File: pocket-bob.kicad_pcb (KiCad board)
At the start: 2 copper layers, 104.1 x 58.4 mm, 131 parts, among them J3 Conn_01x18, J4 Conn_01x18, J5 Conn_01x18, J6 Conn_01x18, J7 USB_A, P1 Conn_02x18_Odd_Even, P2 Conn_02x18_Odd_Even, U1 TPD3S014

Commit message: Some finishing touches
Remove VIN_USB LED.
Give resistors and LEDs some values.
Update the pours.
Update the silkscreen with board revision.
Update all plots.

Signed-off-by: Michael Welling <mwelling79@gmail.com>
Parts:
- removed D4: LED, LED_SMD:LED_0402_1005Metric
- removed R4: R, Resistor_SMD:R_0402_1005Metric
- D1, D25, D30, D43, D45, D48: value LED -> RED
- D10, D11, D12, D13, D14, D15, D16, D17, D18, D19, D20, D21, D22, D23, D24, D27, D28, D31, D32, D33, D34, D35, D36, D37, D38, D39, D40, D41, D42, D46, D49, D50, D51, D52, D53, D54, D55, D56, D57, D58, D59, D63, D64, D65, D66, D68, D69, D70, D71, D72: value LED -> GREEN
- R1: value R -> 2.2K
- R10, R11, R12, R13, R14, R15, R16, R17, R18, R19, R20, R21, R22, R23, R24, R25, R27, R28, R30, R31, R32, R33, R34, R35, R36, R37, R38, R39, R40, R41, R42, R43, R45, R46, R48, R49, R50, R51, R52, R53, R54, R55, R56, R57, R58, R59, R63, R64, R65, R66, R68, R69, R70, R71, R72: value R -> 1K
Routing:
- net /VIN_USB: track 18.7 -> 16.3 mm
- net Net-(D4-A): track 1.52 -> 0.00 mm
- net GND: track 73.2 -> 72.0 mm, vias 61 -> 60
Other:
- board text added: "Pocket-BoB"
- board text added: "R0 - 03/2025"
- board text added: "m_w"

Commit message: Small updates
Switched all 5V LED current limiting resistors to 2.2K.
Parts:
- R25, R48: value 1K -> 2.2K
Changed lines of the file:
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@@
 			)
 		)
-		(property "Value" "1K"
+		(property "Value" "2.2K"
 			(at 0 1.17 0)
 			(layer "F.Fab")
@@
 			)
 		)
-		(property "Value" "1K"
+		(property "Value" "2.2K"
 			(at 0 1.17 0)
 			(layer "F.Fab")

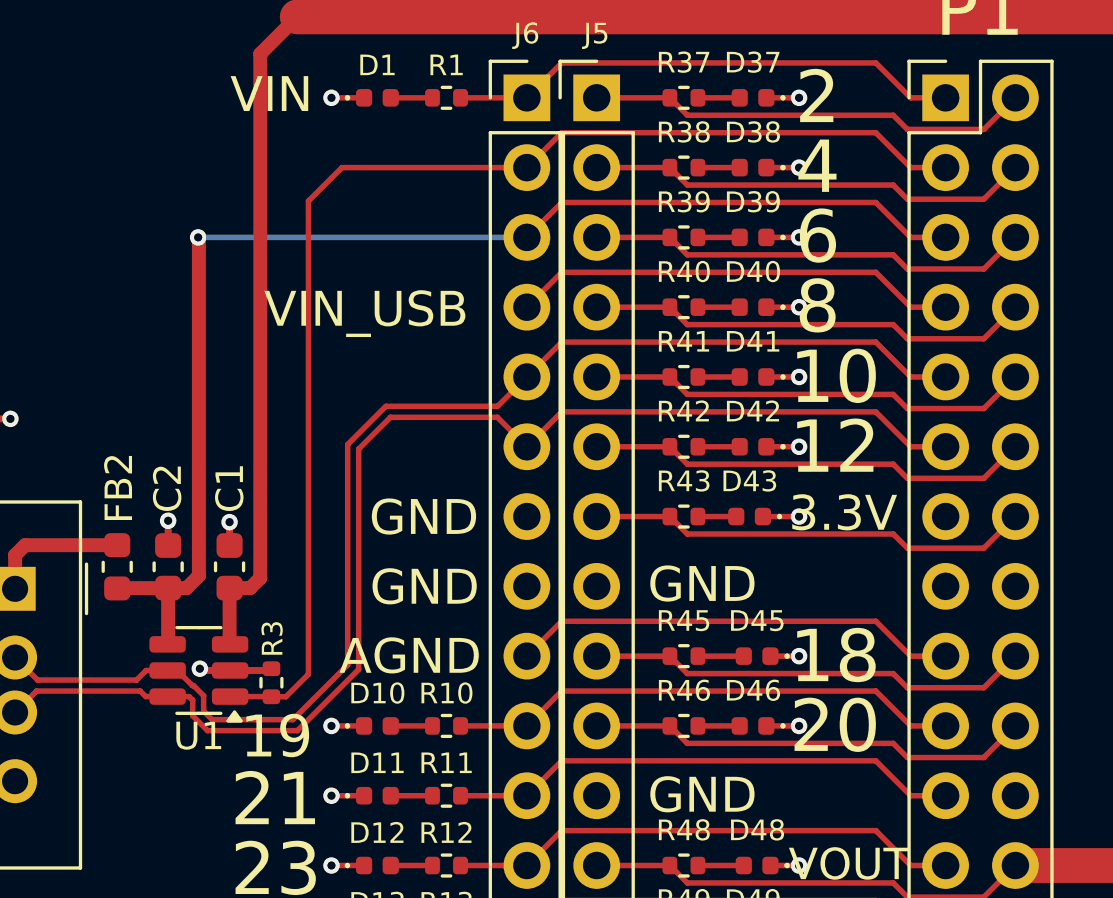
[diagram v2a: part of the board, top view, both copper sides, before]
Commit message: Switch P1_13 to LED instead of GND
The USB_ID functionality is not need if we aren't using OTG.

Signed-off-by: Michael Welling <mwelling79@gmail.com>
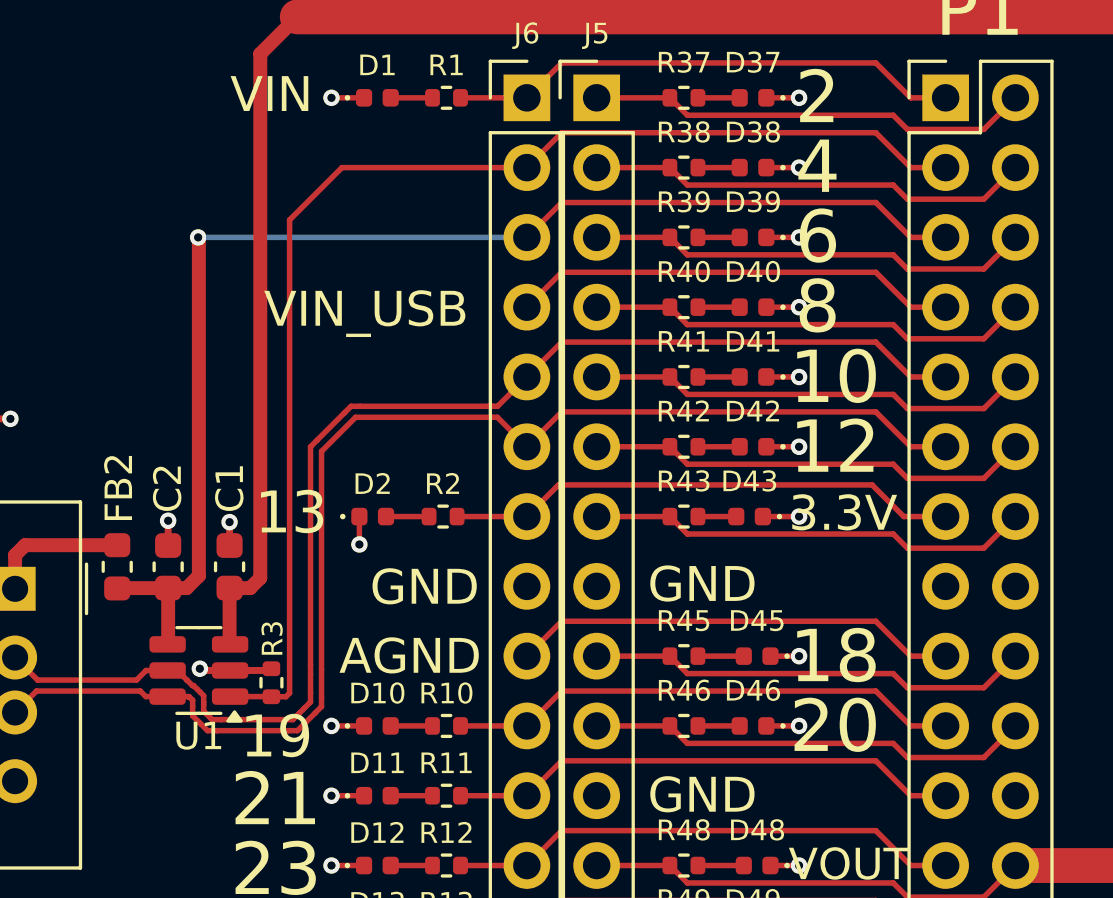
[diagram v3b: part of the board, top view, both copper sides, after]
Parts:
- added D2: GREEN, LED_SMD:LED_0402_1005Metric, F.Cu at (60.4, 83.8)
- added R2: 1K, Resistor_SMD:R_0402_1005Metric, F.Cu at (63.0, 83.8)
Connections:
- J6 pad 7: GND -> /P1_13
- P1 pad 13: GND -> /P1_13
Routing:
- net /P1_13: track 0.00 -> 18.6 mm
- net Net-(D2-A): track 0.00 -> 1.57 mm
- net GND: track 72.0 -> 73.0 mm, vias 60 -> 61
- net /USB1_D-: track 46.3 -> 47.1 mm
- net /USB1_D+: track 46.0 -> 46.8 mm
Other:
- board text added: "13"

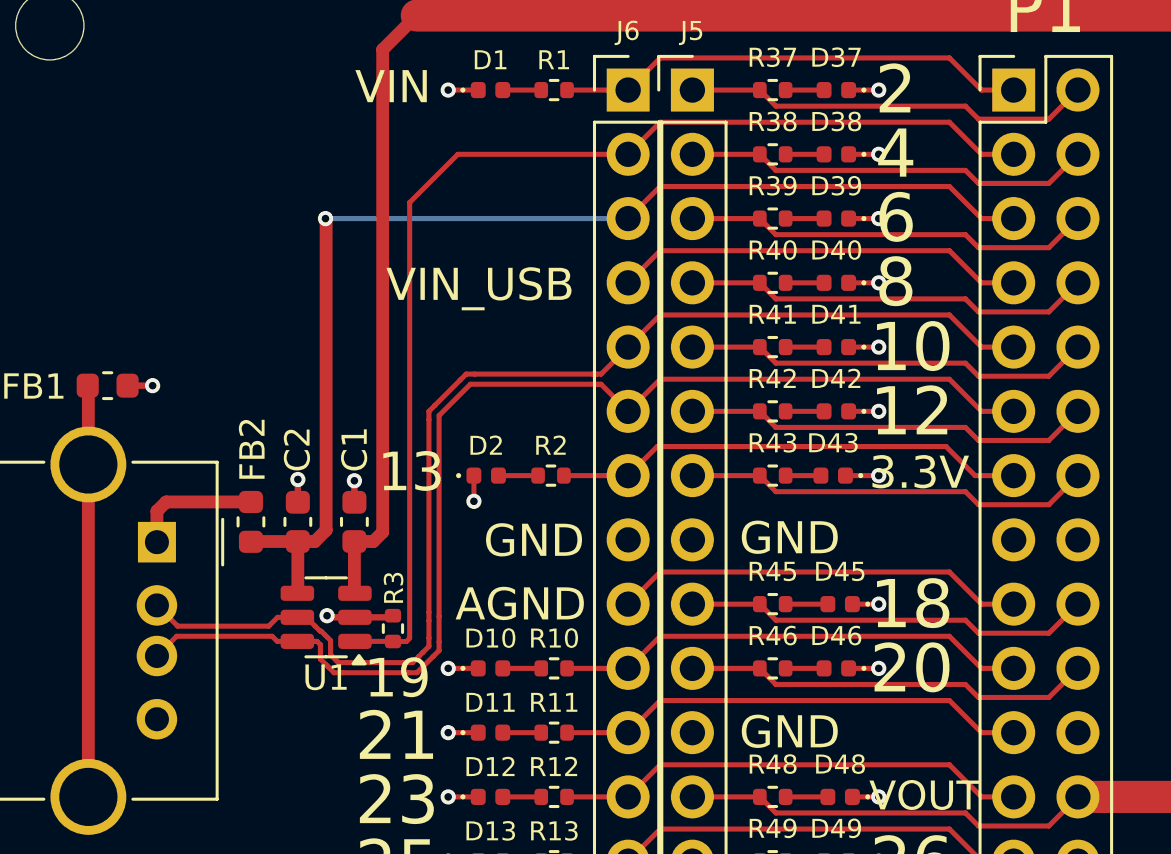
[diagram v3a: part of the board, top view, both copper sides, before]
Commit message: Update diff pairs
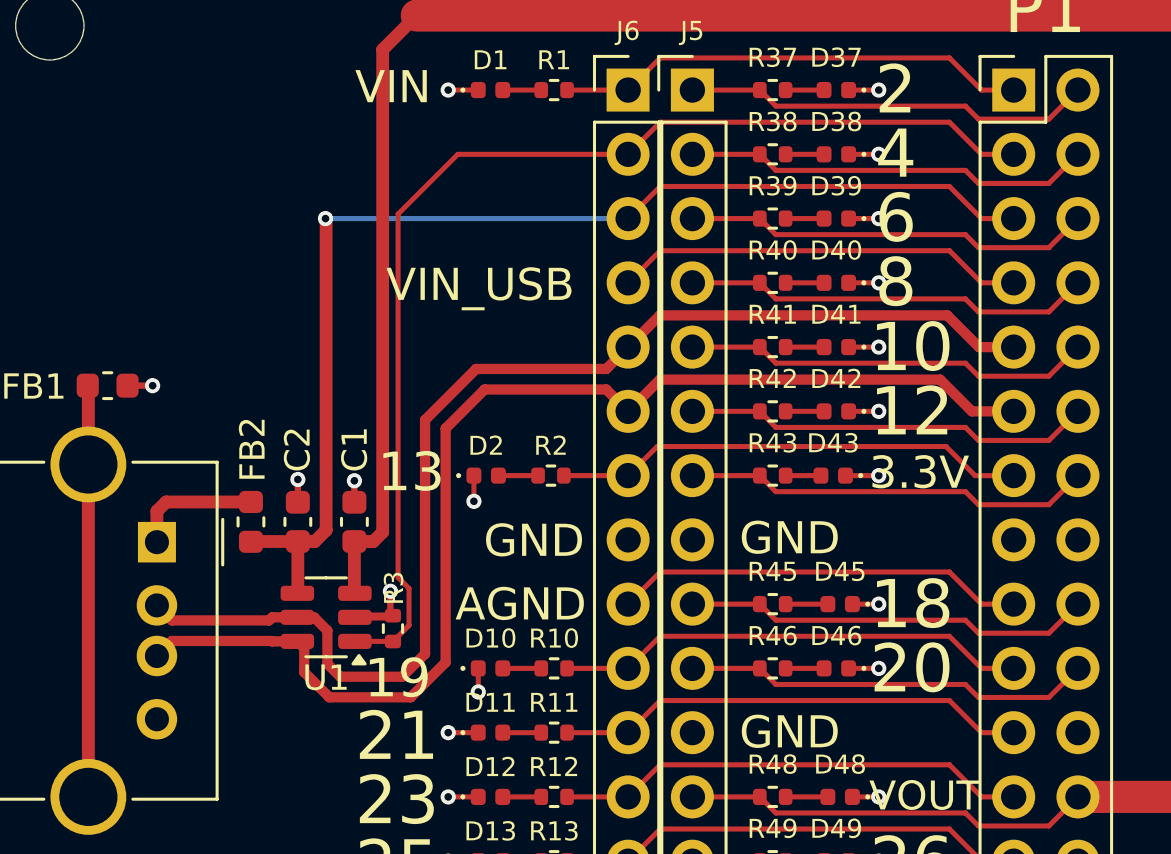
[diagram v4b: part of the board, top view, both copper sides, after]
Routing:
- net GND: track 73.0 -> 74.2 mm
- net /USB1_D-: track 47.1 -> 47.8 mm
- net /USB1_D+: track 46.8 -> 47.4 mm
